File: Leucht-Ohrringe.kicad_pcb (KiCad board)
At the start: 2 copper layers, 20 x 49.5 mm, 46 parts, among them J1 Conn_ARM_SWD_TagConnect_TC2030, P1 USB_C_Plug_USB2.0, U4 CH340N, U5 nRF52832-QFxx

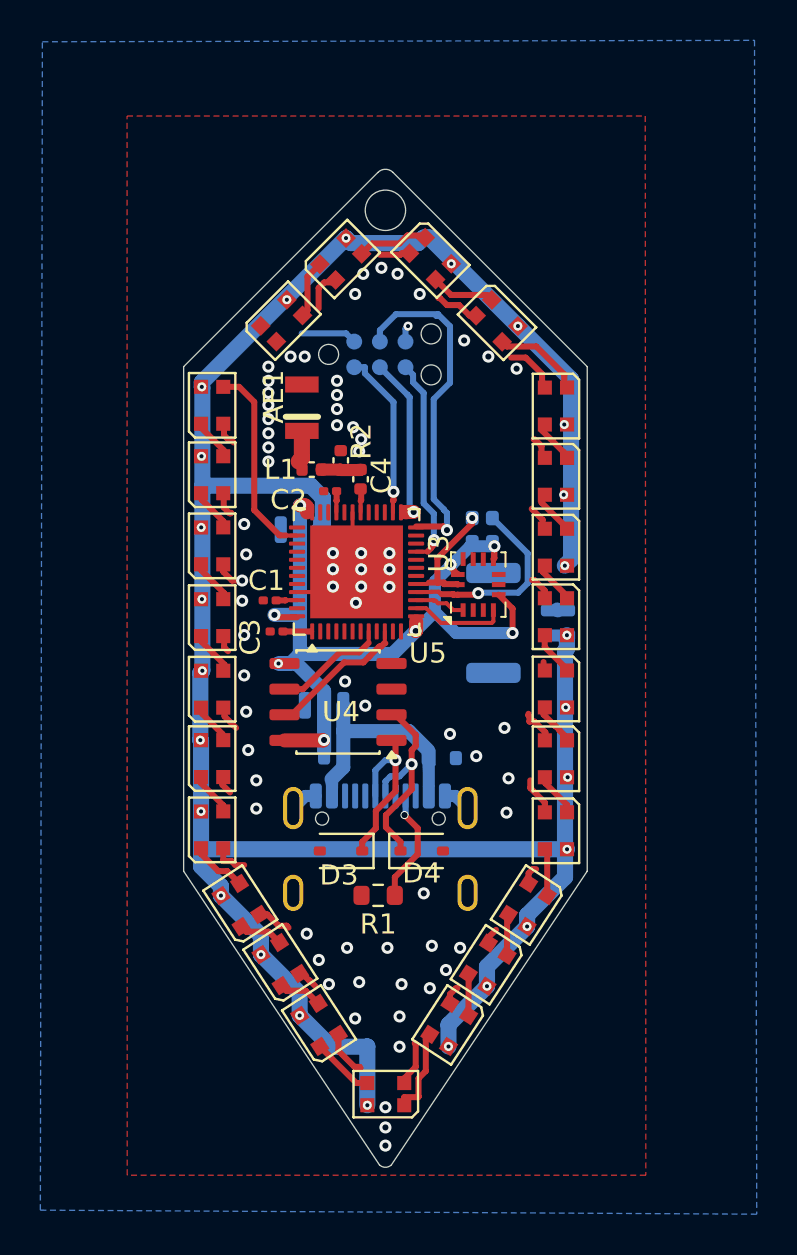
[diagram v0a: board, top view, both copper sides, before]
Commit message: move usb closer to the edge, add ntc
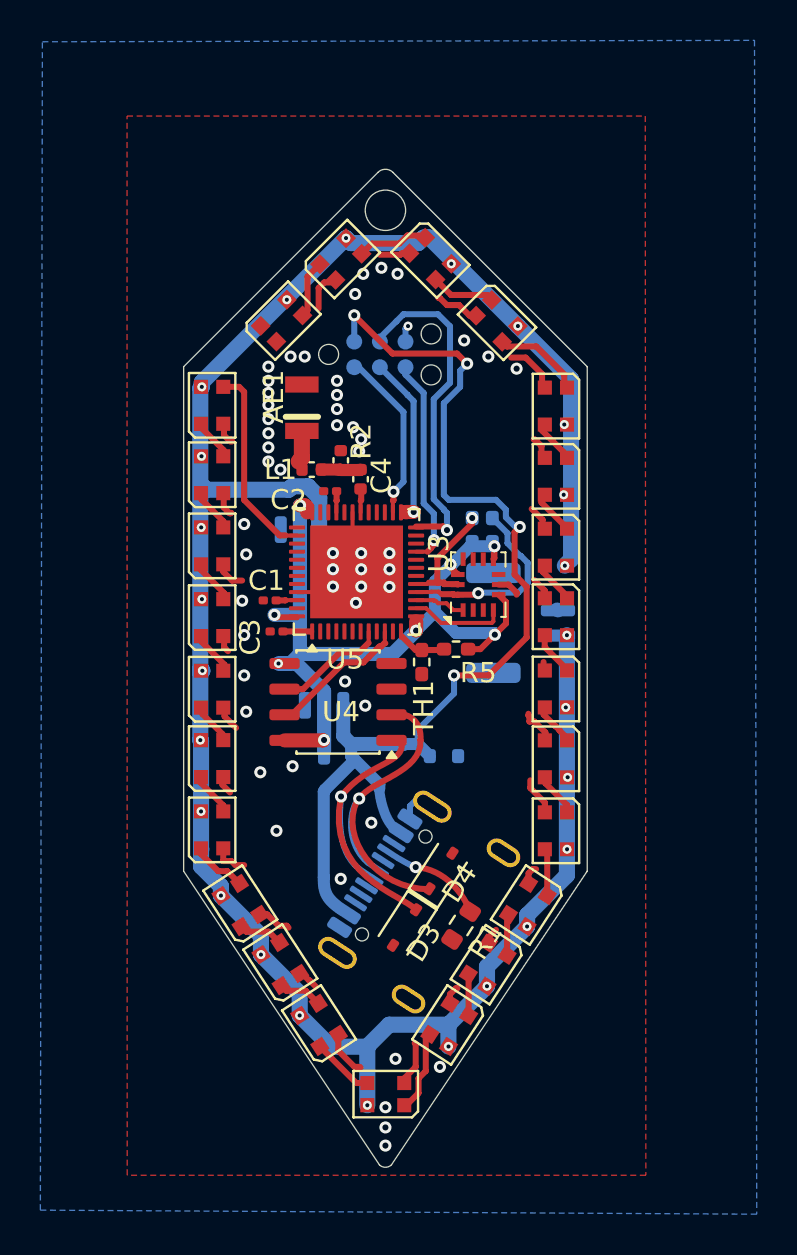
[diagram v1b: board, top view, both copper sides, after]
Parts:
- added R5: 100k, Resistor_SMD:R_0402_1005Metric_Pad0.72x0.64mm_HandSolder, F.Cu at (168.5, 74.0)
- added TH1: Thermistor_NTC, Resistor_SMD:R_0402_1005Metric_Pad0.72x0.64mm_HandSolder, F.Cu at (166.8, 74.6)
- moved D3 4.93 mm to (165.9, 87.8), turned to -123 degrees
- moved R1 4.37 mm to (168.8, 87.7), turned to -123 degrees
- moved P1 3.55 mm to (167.6, 87.1), turned to -123 degrees
- moved D4 1.37 mm to (167.8, 85.0), turned to 57 degrees
- moved D2 0.15 mm to (167.9, 79.3)
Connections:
- J1 pad 1: unconnected-(J1-VCC-Pad1) -> +5V
- U5 pad 12: unconnected-(U5-NFC2/P0.10-Pad12) -> Net-(U5-NFC2/P0.10)
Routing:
- net +5V: track 8.48 -> 49.4 mm, vias 0 -> 4
- net +BATT: track 123.0 -> 109.3 mm
- net /D-: track 11.6 -> 0.97 mm
- net /D+: track 9.02 -> 0.25 mm
- net Net-(P1-CC): track 5.69 -> 0.00 mm
- net unconnected-(J1-VCC-Pad1): track 2.77 -> 0.00 mm
- net Net-(U5-NFC2/P0.10): track 0.00 -> 2.38 mm
- net GND: track 45.5 -> 44.5 mm, vias 71 -> 54
- net VDD: track 40.5 -> 41.4 mm

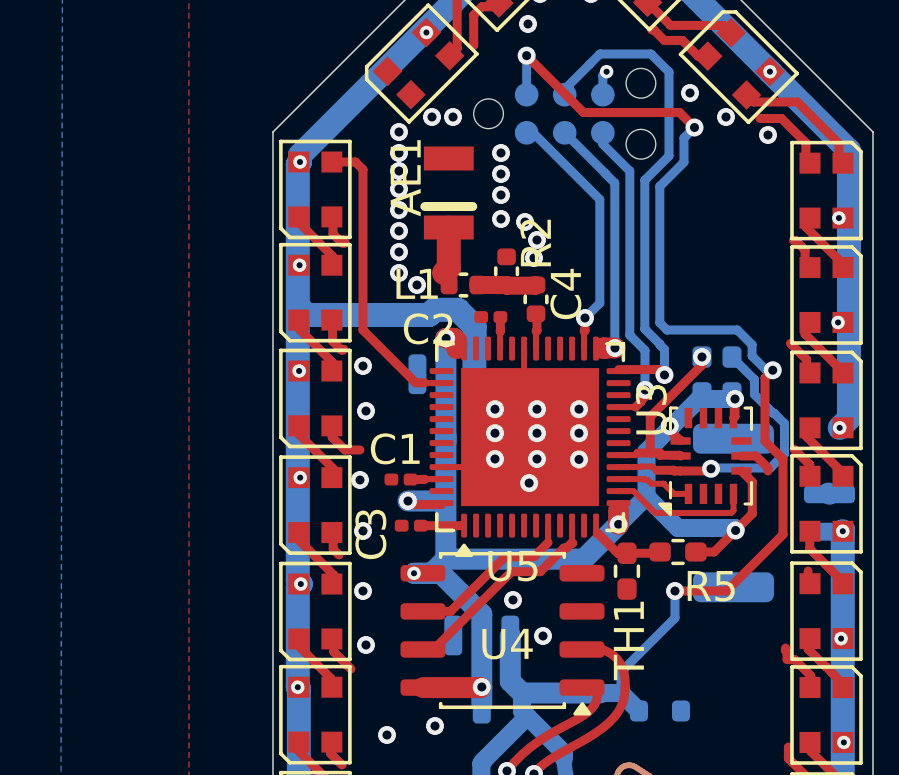
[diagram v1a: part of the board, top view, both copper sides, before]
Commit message: switch some components to jlc basic parts
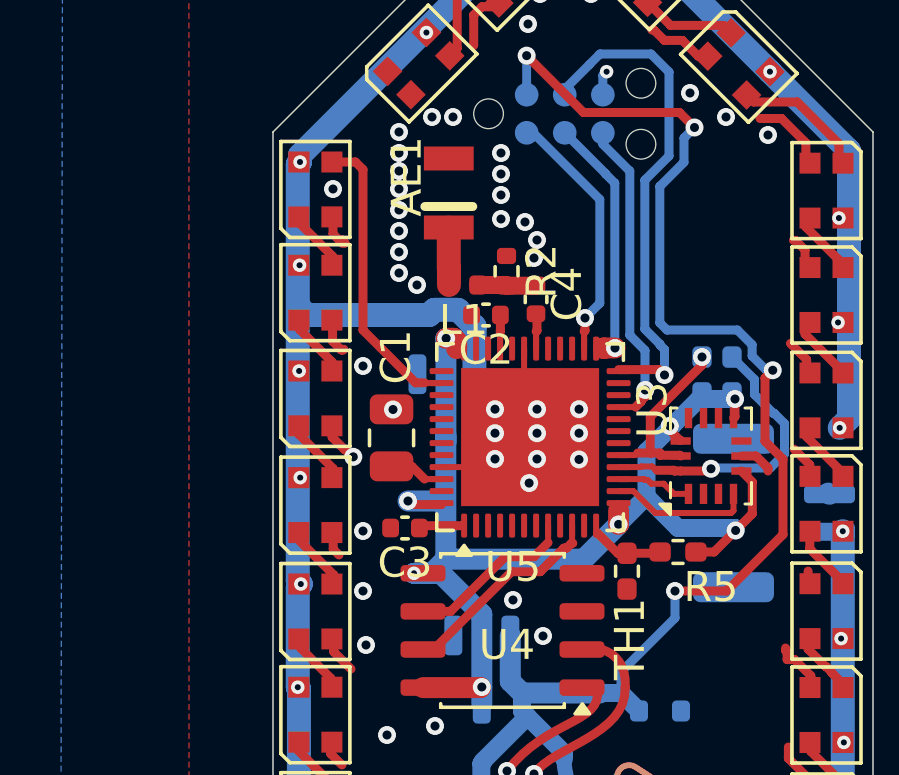
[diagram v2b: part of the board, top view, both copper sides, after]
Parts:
- C1: footprint Capacitor_SMD:C_0201_0603Metric -> Capacitor_SMD:C_0805_2012Metric
- C2, C3: footprint Capacitor_SMD:C_0201_0603Metric -> Capacitor_SMD:C_0402_1005Metric
- L1: value 0 -> 6,8nH; footprint Capacitor_SMD:C_0402_1005Metric -> Inductor_SMD:L_0402_1005Metric
- R2: footprint Capacitor_SMD:C_0402_1005Metric -> Resistor_SMD:R_0402_1005Metric
- U1, U2: value ~ -> TX4204
- U3: value ~ -> ICM-42670-L
- moved C1 1.42 mm to (159.0, 70.2), turned to 90 degrees
- moved C3 0.22 mm to (159.4, 73.2)
- moved C2 0.17 mm to (162.1, 66.1)
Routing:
- net Net-(U5-DEC4): track 1.04 -> 1.79 mm
- net GND: track 44.5 -> 44.4 mm, vias 54 -> 55

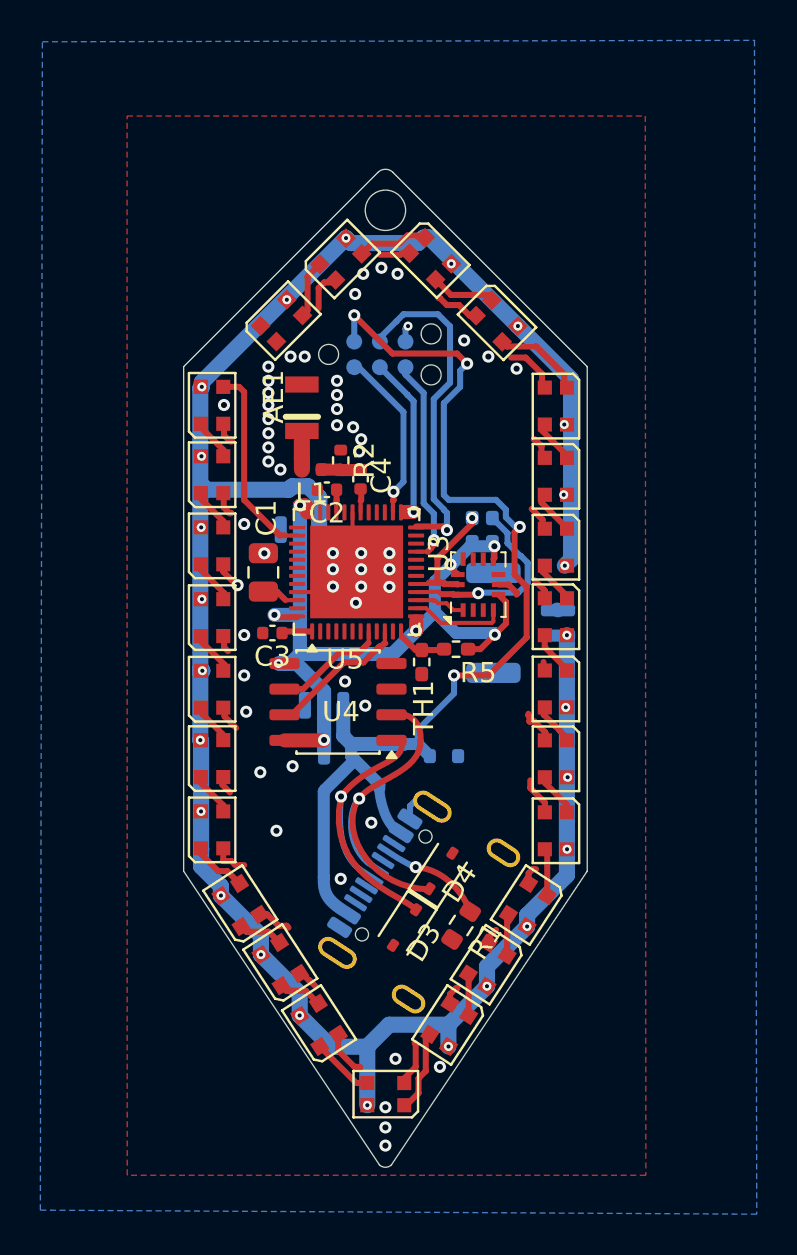
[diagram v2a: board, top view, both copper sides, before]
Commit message: add decoupling caps for icm imu, select smaller footrpint for cap
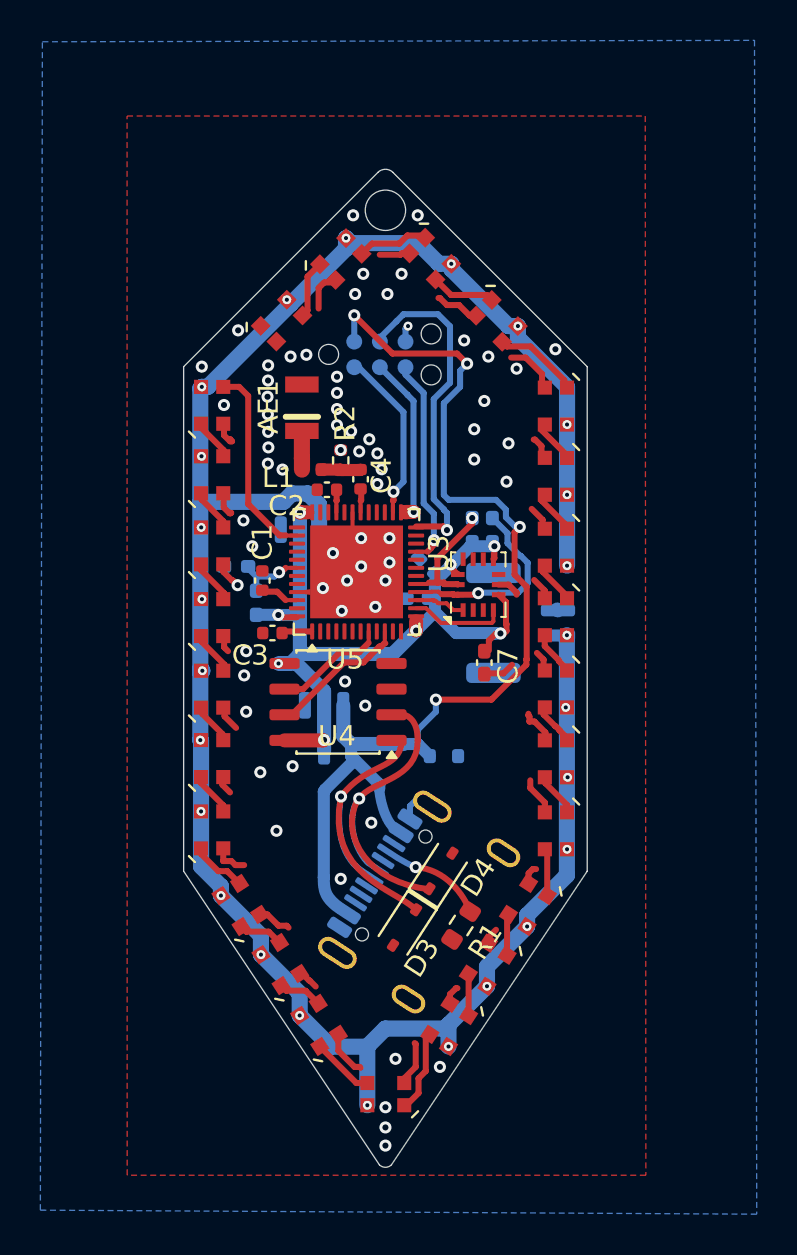
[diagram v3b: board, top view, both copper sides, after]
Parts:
- added C5: 0.1µF, Capacitor_SMD:C_0402_1005Metric_Pad0.74x0.62mm_HandSolder, B.Cu at (166.6, 71.5)
- added C6: 2,2µF, Capacitor_SMD:C_0402_1005Metric_Pad0.74x0.62mm_HandSolder, B.Cu at (167.1, 69.9)
- added C7: 10nF, Capacitor_SMD:C_0402_1005Metric_Pad0.74x0.62mm_HandSolder, F.Cu at (169.9, 74.7)
- C1: footprint Capacitor_SMD:C_0805_2012Metric -> Capacitor_SMD:C_0402_1005Metric
- R5, TH1: moved to B.Cu
- moved TH1 10.3 mm to (157.6, 69.9), turned to 180 degrees
- moved R5 10.2 mm to (158.6, 71.7), turned to 90 degrees
- moved C1 0.41 mm to (158.9, 70.6)
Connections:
- R5 pad 2: Net-(U5-NFC2/P0.10) -> Net-(U5-P0.30/AIN6)
- TH1 pad 1: Net-(U5-NFC2/P0.10) -> Net-(U5-P0.30/AIN6)
- U5 pad 12: Net-(U5-NFC2/P0.10) -> unconnected-(U5-NFC2/P0.10-Pad12)
- U5 pad 42: unconnected-(U5-P0.30/AIN6-Pad42) -> Net-(U5-P0.30/AIN6)
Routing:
- net Net-(U5-P0.30/AIN6): track 0.00 -> 3.49 mm, vias 0 -> 1
- net Net-(U5-NFC2/P0.10): track 2.38 -> 0.00 mm
- net +5V: track 49.4 -> 50.0 mm
- net GND: track 44.4 -> 44.3 mm, vias 55 -> 68
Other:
- board text added: "5V"
- board text removed: "VDD"

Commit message: fix buck converter circuit, add switch for 5V usb/off/swd power and bat power
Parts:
- removed U2: TX4204, Package_TO_SOT_SMD:SOT-23-3
- added C8: 100µF, Capacitor_SMD:C_1206_3216Metric_Pad1.33x1.80mm_HandSolder, B.Cu at (157.4, 73.0)
- added C9: 10µF, Capacitor_SMD:C_0603_1608Metric_Pad1.08x0.95mm_HandSolder, B.Cu at (167.4, 77.3)
- added L2: 22µH, Inductor_SMD:FNR3015S, B.Cu at (162.9, 78.5)
- added SW1: SW_SPDT, Inductor_SMD:K3-1236S, B.Cu at (158.2, 80.0)
- moved U1 6.45 mm to (163.8, 74.9), turned to 90 degrees
- moved TH1 0.80 mm to (158.4, 69.9)
- moved R5 0.51 mm to (159.1, 71.6)
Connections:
- U1 pad 2: +BATT -> Net-(U1-SW)
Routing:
- net +BATT: track 109.2 -> 117.9 mm
- net Net-(SW1-B): track 0.00 -> 8.63 mm
- net +5V: track 50.0 -> 46.1 mm
- net Net-(U1-SW): track 0.00 -> 2.37 mm
- net GND: track 44.3 -> 46.3 mm, vias 68 -> 73
- net Net-(U4-TXD): track 5.99 -> 7.00 mm
- net Net-(U4-RXD): track 7.36 -> 8.38 mm
- net VDD: track 41.5 -> 42.1 mm

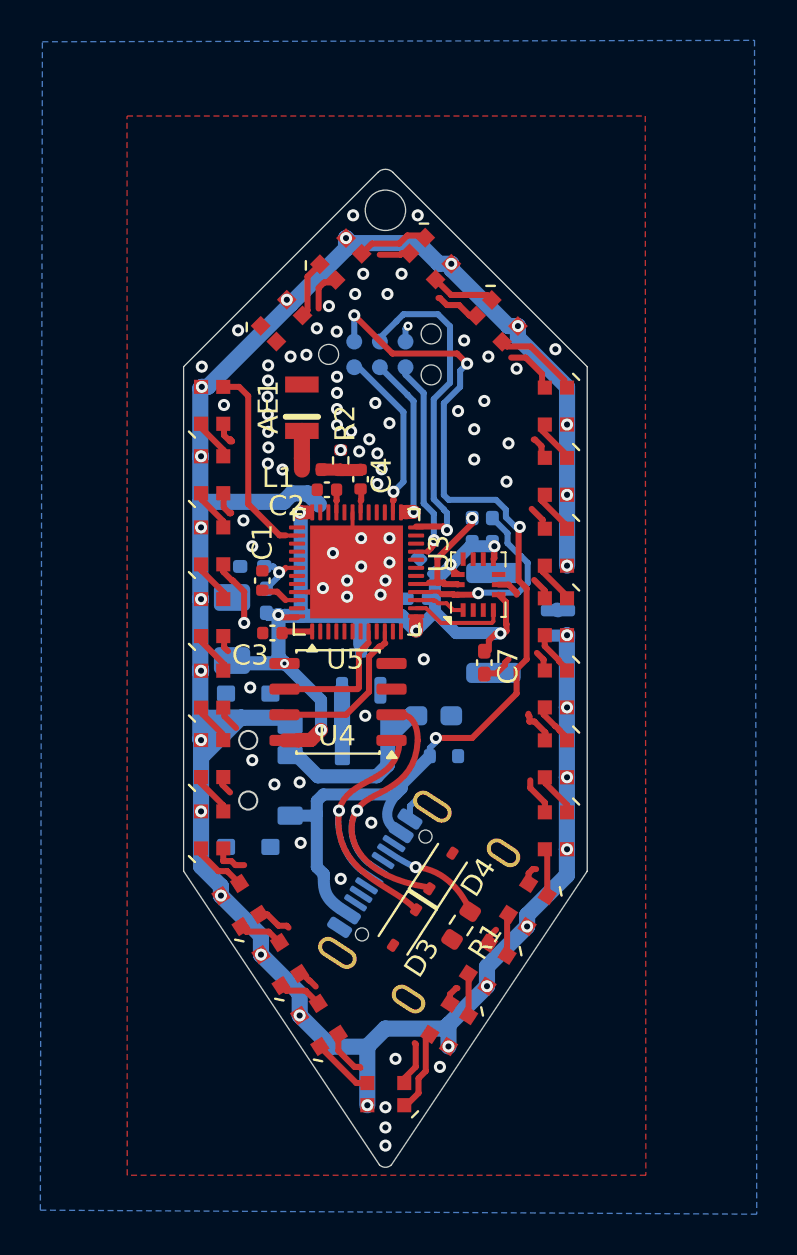
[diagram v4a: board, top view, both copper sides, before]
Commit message: fix CH340N, add pads for gpios, add switch model
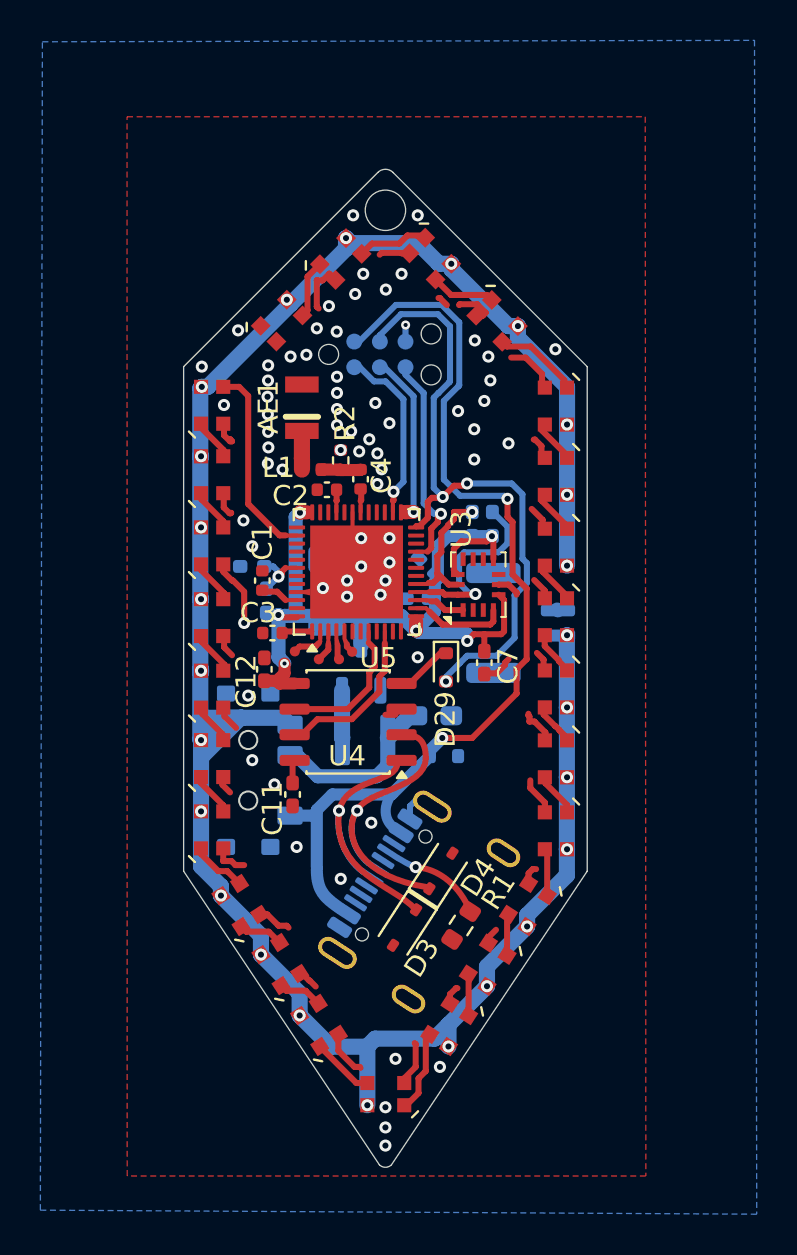
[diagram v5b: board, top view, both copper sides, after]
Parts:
- added C11: 0.1µF, Capacitor_SMD:C_0402_1005Metric_Pad0.74x0.62mm_HandSolder, F.Cu at (160.4, 81.2)
- added C12: 0.1µF, Capacitor_SMD:C_0402_1005Metric_Pad0.74x0.62mm_HandSolder, F.Cu at (159.0, 75.0)
- added D29: B0520, Diode_SMD:D_SOD-523, F.Cu at (168.0, 74.9)
- added TP1: TestPoint, Inductor_SMD:TestPoint_0,5mm, F.Cu at (160.5, 74.1)
- added TP2: TestPoint, Inductor_SMD:TestPoint_0,5mm, F.Cu at (161.7, 74.5)
- added TP3: TestPoint, Inductor_SMD:TestPoint_0,5mm, F.Cu at (162.7, 74.5)
- added TP4: TestPoint, Inductor_SMD:TestPoint_0,5mm, F.Cu at (163.3, 74.1)
- moved C8 5.05 mm to (162.1, 71.1)
- moved U4 1.11 mm to (163.2, 77.6)
- moved R3 0.30 mm to (169.3, 67.8)
- moved R4 0.30 mm to (170.3, 67.8)
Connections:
- net Net-(J1-~{RESET}) renamed RESET
- U4 pad 4: unconnected-(U4-~{RTS}-Pad4) -> Net-(D29-K)
- U4 pad 8: VDD -> Net-(U4-V3)
- U5 pad 2: unconnected-(U5-P0.00/XL1-Pad2) -> Net-(U5-P0.00/XL1)
- U5 pad 3: unconnected-(U5-P0.01/XL2-Pad3) -> Net-(U5-P0.01/XL2)
- U5 pad 4: unconnected-(U5-P0.02/AIN0-Pad4) -> Net-(U5-P0.02/AIN0)
- U5 pad 5: unconnected-(U5-P0.03/AIN1-Pad5) -> Net-(U5-P0.03/AIN1)
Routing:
- net RESET: track 16.9 -> 32.2 mm, vias 1 -> 3
- net +BATT: track 117.9 -> 111.6 mm
- net Net-(D29-K): track 0.00 -> 2.82 mm
- net GND: track 46.3 -> 48.6 mm, vias 73 -> 69
- net Net-(U5-P0.00/XL1): track 0.00 -> 1.97 mm
- net Net-(U5-P0.01/XL2): track 0.00 -> 1.43 mm
- net +5V: track 46.1 -> 44.9 mm, vias 4 -> 2
- net Net-(U4-V3): track 0.00 -> 1.16 mm
- net VDD: track 42.1 -> 41.0 mm, vias 8 -> 6
- net /D-: track 0.97 -> 0.00 mm
- net Net-(U3-AP_SCL): track 6.01 -> 6.87 mm
- net Net-(U5-P0.02/AIN0): track 0.00 -> 0.76 mm
